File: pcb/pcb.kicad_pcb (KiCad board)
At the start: 2 copper layers, 129 x 93.3 mm, 53 parts, among them J1 MJ-4PP-9, SW1 SW_PUSH, SW10 SW_PUSH, SW11 SW_PUSH, SW12 SW_PUSH, SW13 SW_PUSH, SW14 SW_PUSH, SW15 SW_PUSH, SW16 SW_PUSH, SW17 SW_PUSH, SW18 SW_PUSH, SW2 SW_PUSH, SW3 SW_PUSH, SW4 SW_PUSH, SW5 SW_PUSH, SW6 SW_PUSH, SW7 SW_PUSH, SW8 SW_PUSH, SW9 SW_PUSH, U1 xiao-ble, U2 xiao-ble

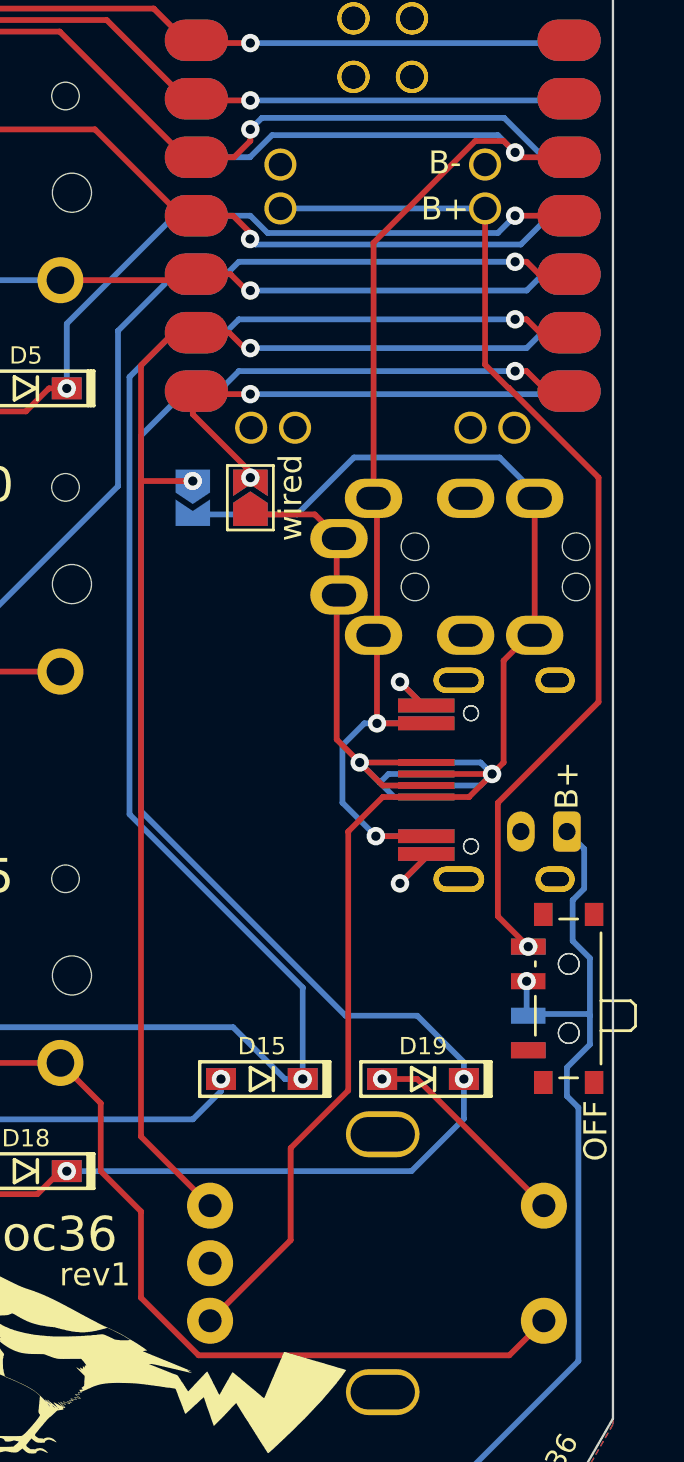
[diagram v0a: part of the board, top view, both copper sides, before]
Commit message: move usb-c connector a bit
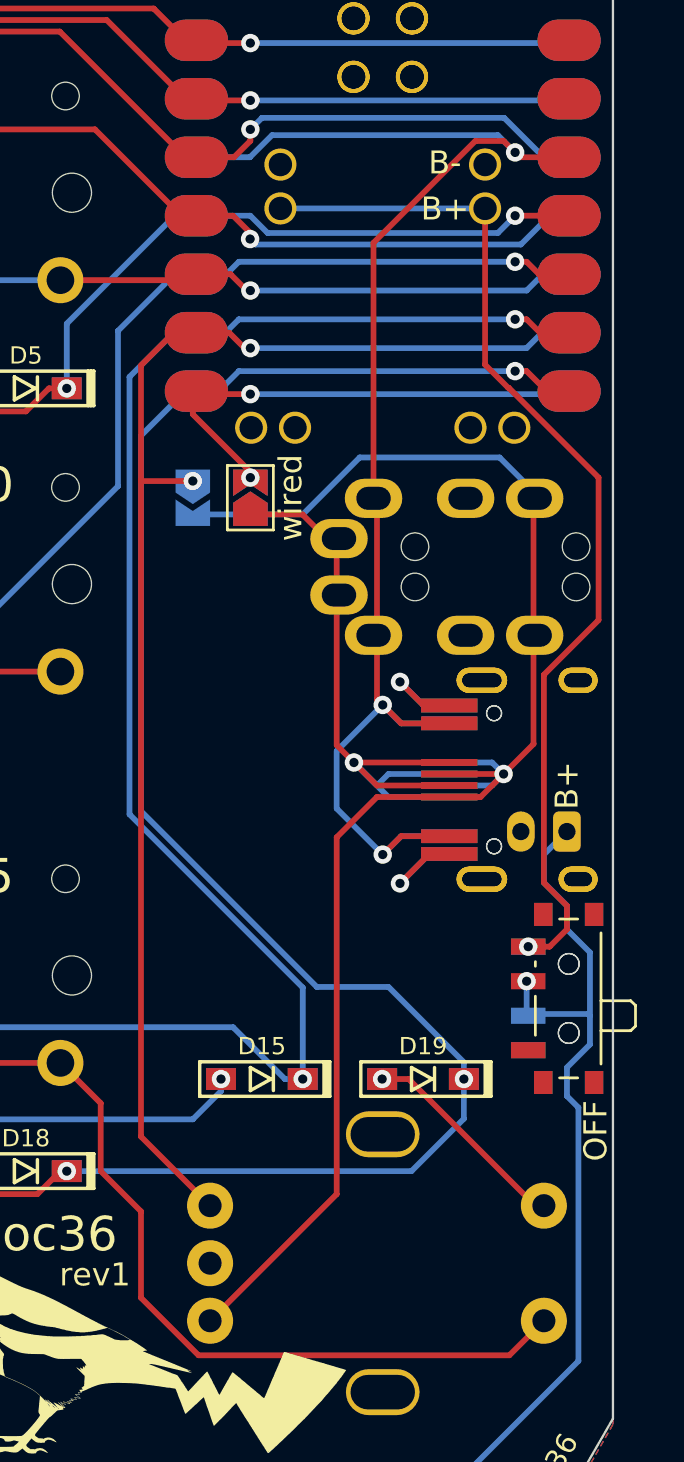
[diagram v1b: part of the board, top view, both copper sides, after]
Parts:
- moved USB1 1.00 mm to (180.6, 84.5)
- moved USB2 1.00 mm to (180.6, 84.5)
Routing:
- net DATA: track 26.1 -> 28.2 mm
- net ENCB: track 69.5 -> 71.4 mm
- net VCC: track 62.3 -> 63.4 mm

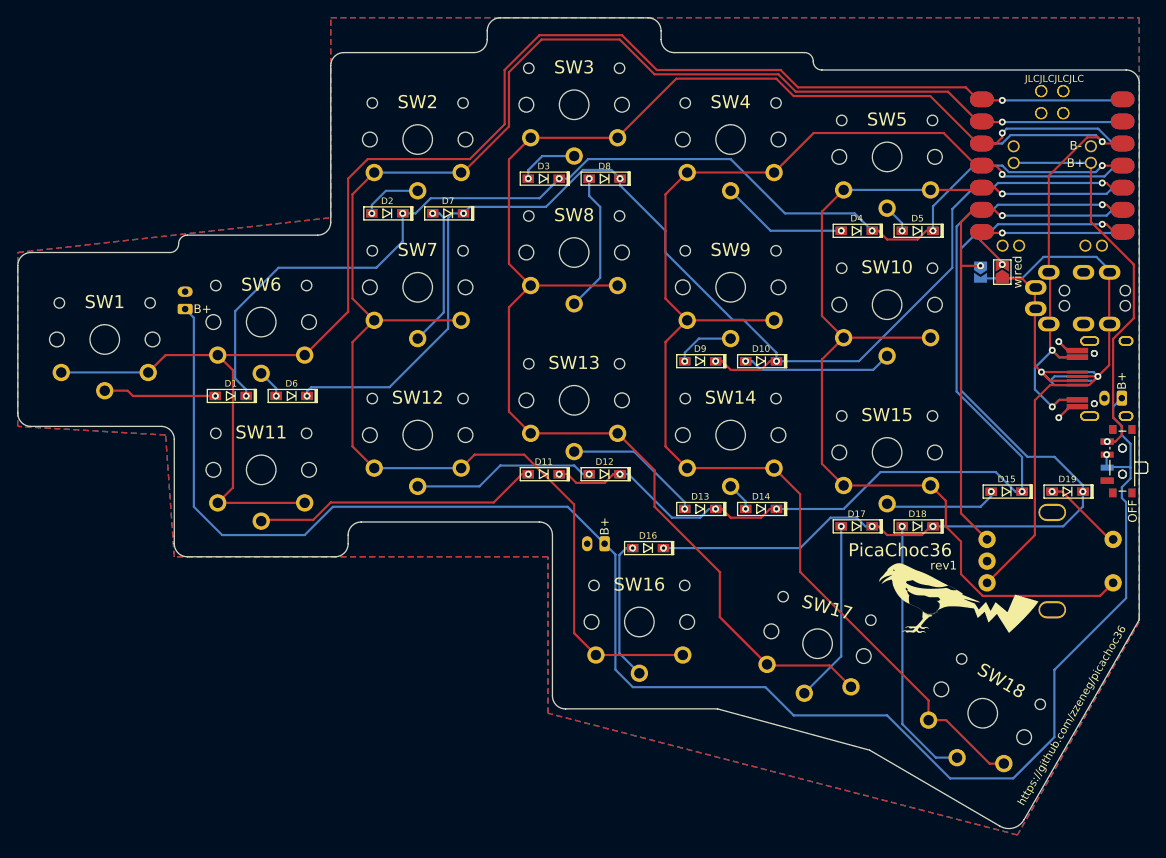
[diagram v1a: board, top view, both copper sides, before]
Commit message: fix choc footprint
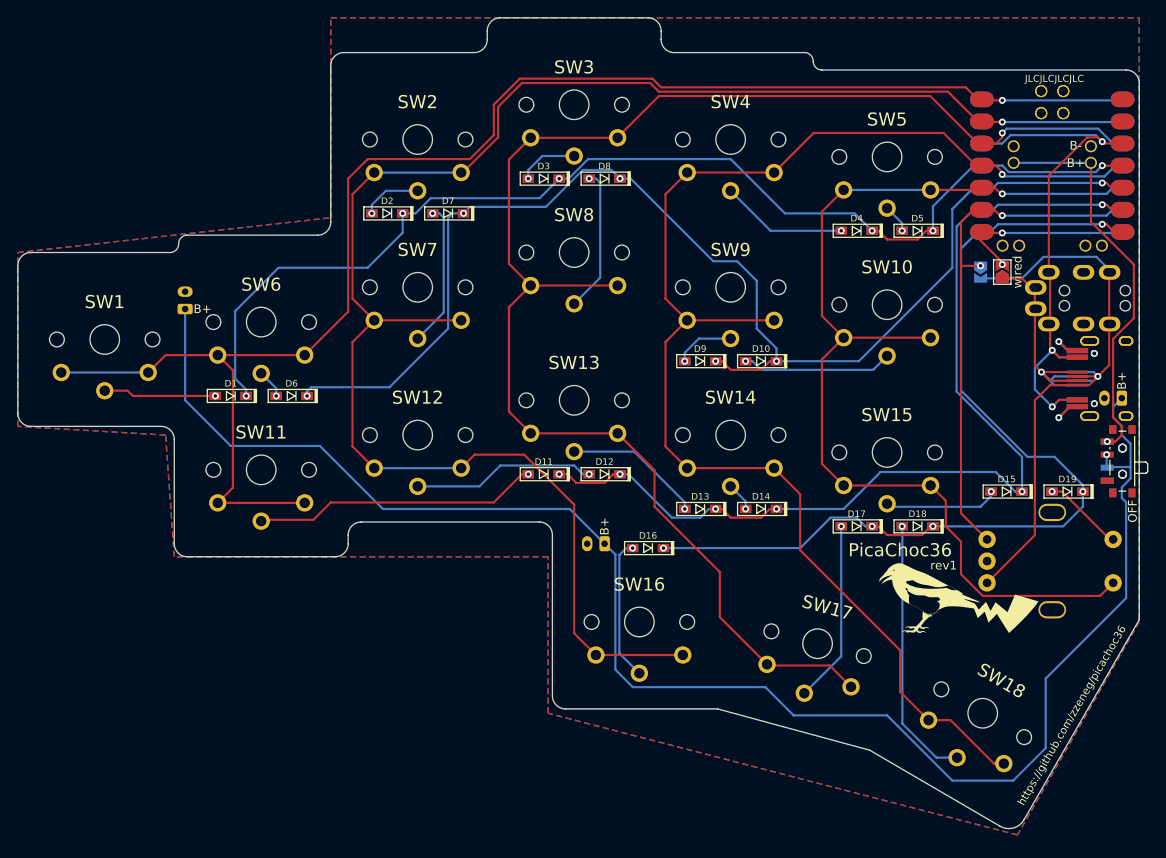
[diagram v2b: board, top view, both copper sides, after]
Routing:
- net BATT: track 196.2 -> 187.2 mm
- net col1: track 203.0 -> 197.3 mm
- net col0: track 182.9 -> 177.1 mm
- net col2: track 178.8 -> 177.1 mm
- net row1: track 144.9 -> 146.5 mm
- net row0: track 131.6 -> 131.0 mm

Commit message: Revert "fix choc footprint"
This reverts commit fcca782c8e4dbdc4b8a54a5bbd694bc51ef22255.
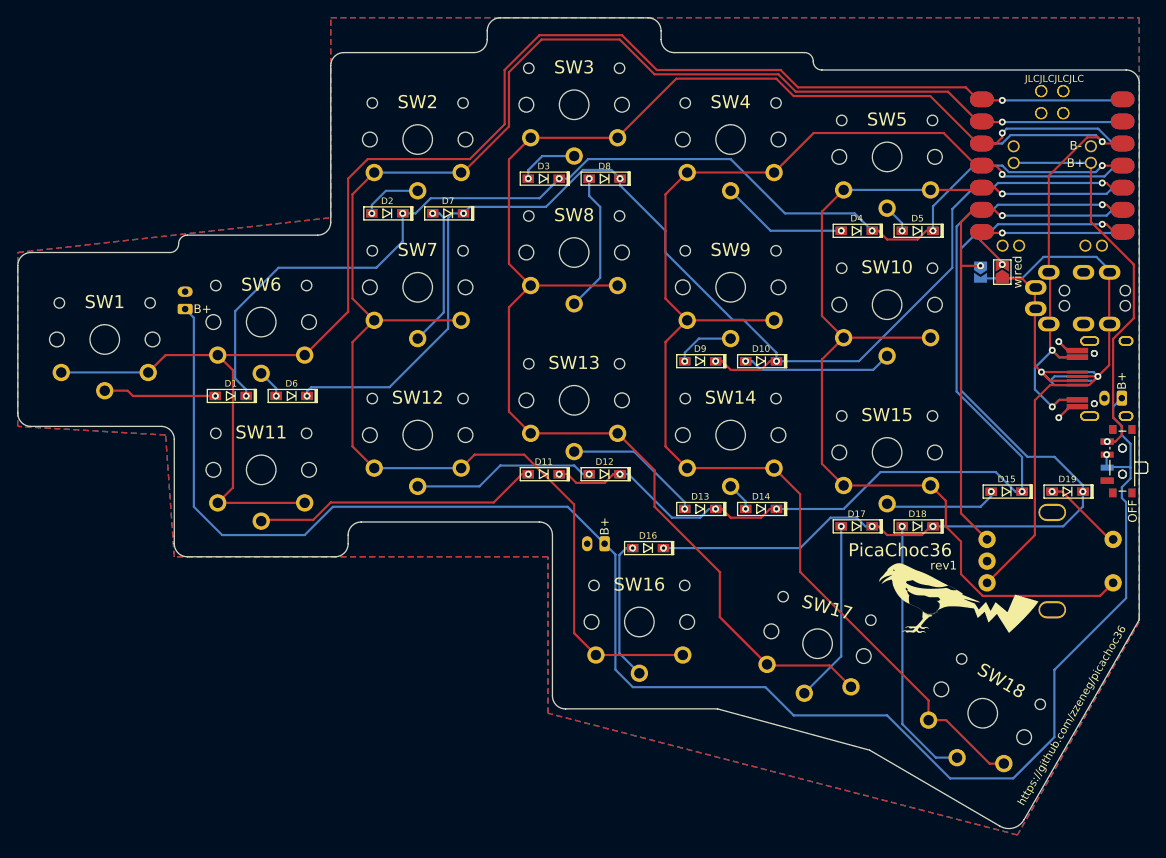
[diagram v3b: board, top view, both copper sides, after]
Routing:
- net BATT: track 187.2 -> 196.2 mm
- net col1: track 197.3 -> 203.0 mm
- net col0: track 177.1 -> 182.9 mm
- net col2: track 177.1 -> 178.8 mm
- net row1: track 146.5 -> 144.9 mm
- net row0: track 131.0 -> 131.6 mm

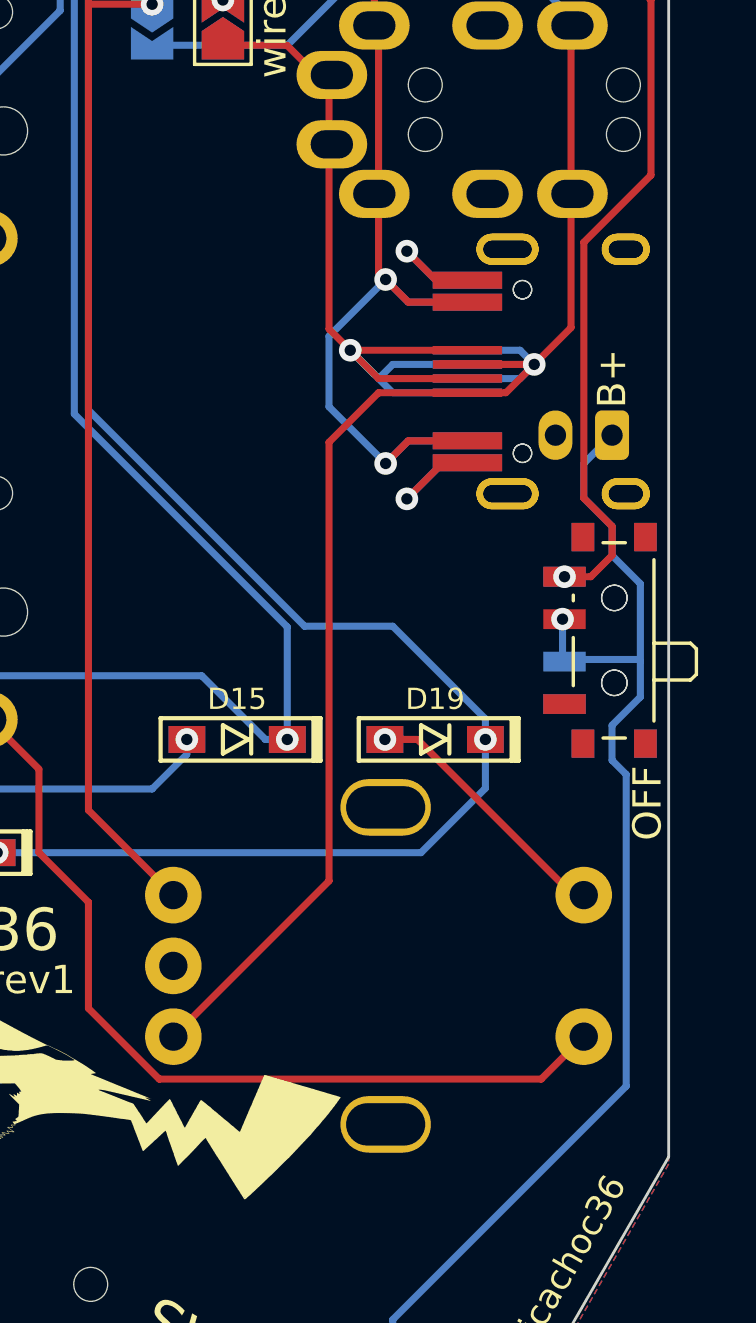
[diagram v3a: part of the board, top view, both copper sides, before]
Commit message: migrate to my own library
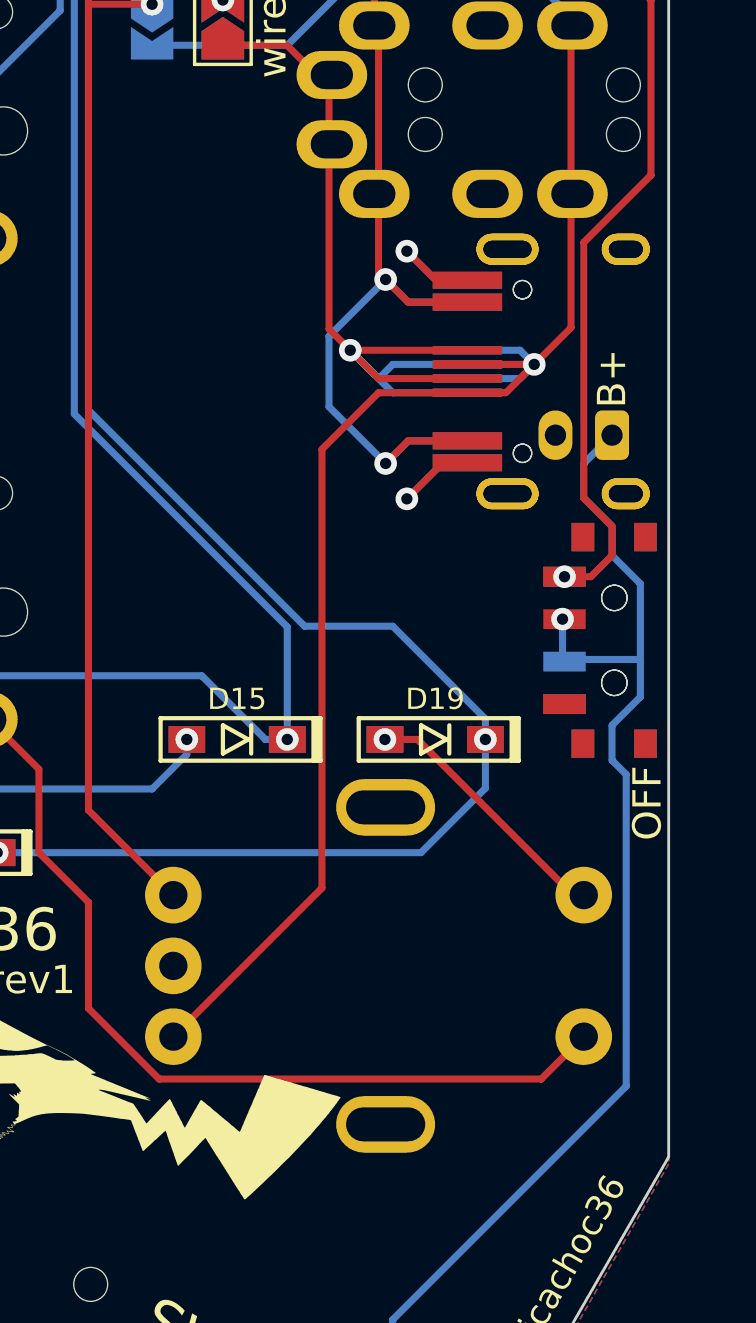
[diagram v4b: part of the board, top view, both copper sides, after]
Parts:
- BATTCONN1, BATTCONN2, BATTCONN3: footprint picachoc:JST_PH_S2B-PH-K_1x02_P2.00mm -> zzkeeb:Connector_JST-1x02-2.00mm
- BATTSW1, BATTSW2: footprint Button_Switch_SMD:SW_SPDT_PCM12 -> zzkeeb:Switch_SPDT-PCM12
- D1, D10, D11, D12, D13, D14, D15, D16, D17, D18, D19, D2, D3, D4, D5, D6, D7, D8, D9: footprint picachoc:D3_SMD -> zzkeeb:Diode_1N4148-SOD123-reversible
- G***: footprint picachoc:logo -> zzkeeb:Logo_pica
- G***: footprint picachoc:logo_mirror -> zzkeeb:Logo_pica-mirrored
- J1: footprint picachoc:MJ-4PP-9 -> zzkeeb:Connector_TRRS-reversible
- RE1: footprint picachoc:RotaryEncoder_EC11 -> zzkeeb:RotaryEncoder_EC11-reversible
- SW1, SW10, SW11, SW12, SW13, SW14, SW15, SW16, SW17, SW18, SW2, SW3, SW4, SW5, SW6, SW7, SW8, SW9: footprint picachoc:Kailh-PG1350-1u -> zzkeeb:Switch_ChocV1-reversible
- U1, U2: footprint picachoc:xiao-ble-smd -> zzkeeb:MCU_xiao-ble-smd
- USB1, USB2: footprint picachoc:HRO-TYPE-C-31-M-12-data -> zzkeeb:Connector_HRO-TYPE-C-31-M-12-data
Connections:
- net SW_ENCB renamed col4
